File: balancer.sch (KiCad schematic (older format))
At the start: 0 parts

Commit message: added hierarchical sheets and an xh connector
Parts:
- added J1: S4B-XH-SM4-TB, symbol S4B-XH-SM4-TB
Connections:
- new net Cell1+: J1.1
- new net Cell2+: J1.2
- new net Cell3+: J1.3
- new net Cell3-: J1.4
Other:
- note added: "XH Connector"
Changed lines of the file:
@@
 $Descr A4 11693 8268
 encoding utf-8
-Sheet 1 1
+Sheet 1 4
 Title ""
 Date ""
@@
 Comment4 ""
 $EndDescr
+Text Notes 8220 1660 0    60   ~ 0
+XH Connector
+$Sheet
+S 7820 2970 990  380
+U 58CDAE41
+F0 "Cell1" 60
+F1 "CellBalancer.sch" 60
+F2 "Cell+" I R 8810 3040 60
+F3 "Cell-" I R 8810 3280 60
+F4 "Reference" O R 8810 3200 60
+F5 "Undervoltage" O R 8810 3120 60
+$EndSheet
+Text Label 9000 3040 0    60   ~ 0
+Cell1+
+Wire Wire Line
+	8810 3040 9000 3040
+Text Label 8700 1780 2    60   ~ 0
+Cell1+
+Wire Wire Line
+	8700 1780 8760 1780
+$Comp
+L S4B-XH-SM4-TB J1
+U 1 1 58CD24F2
+P 8890 1890
+F 0 "J1" H 8890 2060 60  0000 C CNN
+F 1 "S4B-XH-SM4-TB" H 8870 1680 60  0000 C CNN
+F 2 "" H 8790 1960 60  0001 C CNN
+F 3 "http://www.jst-mfg.com/product/pdf/eng/eXH.pdf" H 8900 1660 60  0001 C CNN
+	1    8890 1890
+	1    0    0    -1
+$EndComp
+$Sheet
+S 7820 3520 990  380
+U 58CDE744
+F0 "Cell2" 60
+F1 "CellBalancer.sch" 60
+F2 "Cell+" I R 8810 3590 60
+F3 "Cell-" I R 8810 3830 60
+F4 "Reference" O R 8810 3750 60
+F5 "Undervoltage" O R 8810 3670 60
+$EndSheet
+Text Label 9000 3590 0    60   ~ 0
+Cell2+
+Wire Wire Line
+	8810 3590 9000 3590
+Wire Wire Line
+	8810 3280 8870 3280
+Wire Wire Line
+	8870 3280 8870 3590
+Connection ~ 8870 3590
+$Sheet
+S 7820 4070 990  380
+U 58CE2F03
+F0 "Cell3" 60
+F1 "CellBalancer.sch" 60
+F2 "Cell+" I R 8810 4140 60
+F3 "Cell-" I R 8810 4380 60
+F4 "Reference" O R 8810 4300 60
+F5 "Undervoltage" O R 8810 4220 60
+$EndSheet
+Text Label 9000 4140 0    60   ~ 0
+Cell3+
+Wire Wire Line
+	9000 4140 8810 4140
+Wire Wire Line
+	8810 3830 8870 3830
+Wire Wire Line
+	8870 3830 8870 4140
+Connection ~ 8870 4140
+Text Label 9000 4380 0    60   ~ 0
+Cell3-
+Wire Wire Line
+	9000 4380 8810 4380
+Text Label 9000 3120 0    60   ~ 0
+Cell1-Undervoltage
+Text Label 9000 3200 0    60   ~ 0
+Cell1-Reference
+Wire Wire Line
+	8810 3120 9000 3120
+Wire Wire Line
+	9000 3200 8810 3200
+Text Label 9000 3670 0    60   ~ 0
+Cell2-Undervoltage
+Text Label 9000 3750 0    60   ~ 0
+Cell2-Reference
+Text Label 9000 4220 0    60   ~ 0
+Cell3-Undervoltage
+Text Label 9000 4300 0    60   ~ 0
+Cell3-Reference
+Wire Wire Line
+	9000 4220 8810 4220
+Wire Wire Line
+	9000 4300 8810 4300
+Wire Wire Line
+	8810 3670 9000 3670
+Wire Wire Line
+	9000 3750 8810 3750
+Text Label 8700 1850 2    60   ~ 0
+Cell2+
+Text Label 8700 1930 2    60   ~ 0
+Cell3+
+Text Label 8700 2000 2    60   ~ 0
+Cell3-
+Wire Wire Line
+	8700 1850 8760 1850
+Wire Wire Line
+	8700 1930 8760 1930
+Wire Wire Line
+	8700 2000 8760 2000
 $EndSCHEMATC

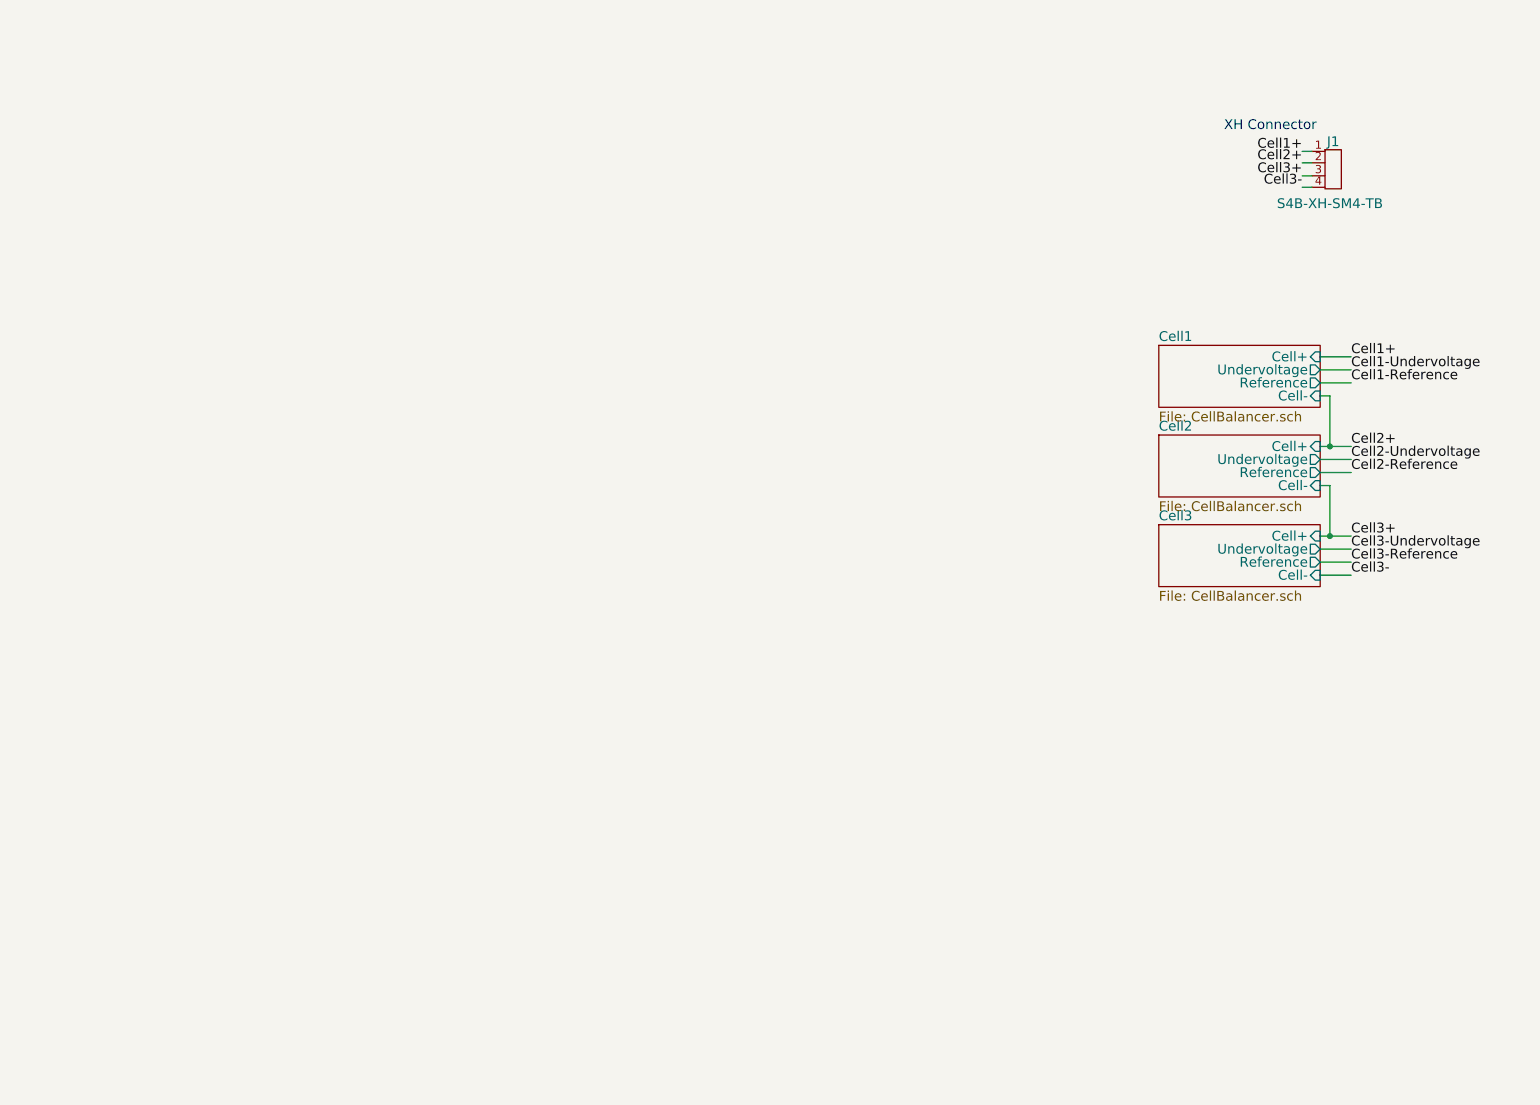
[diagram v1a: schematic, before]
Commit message: high voltage protection done
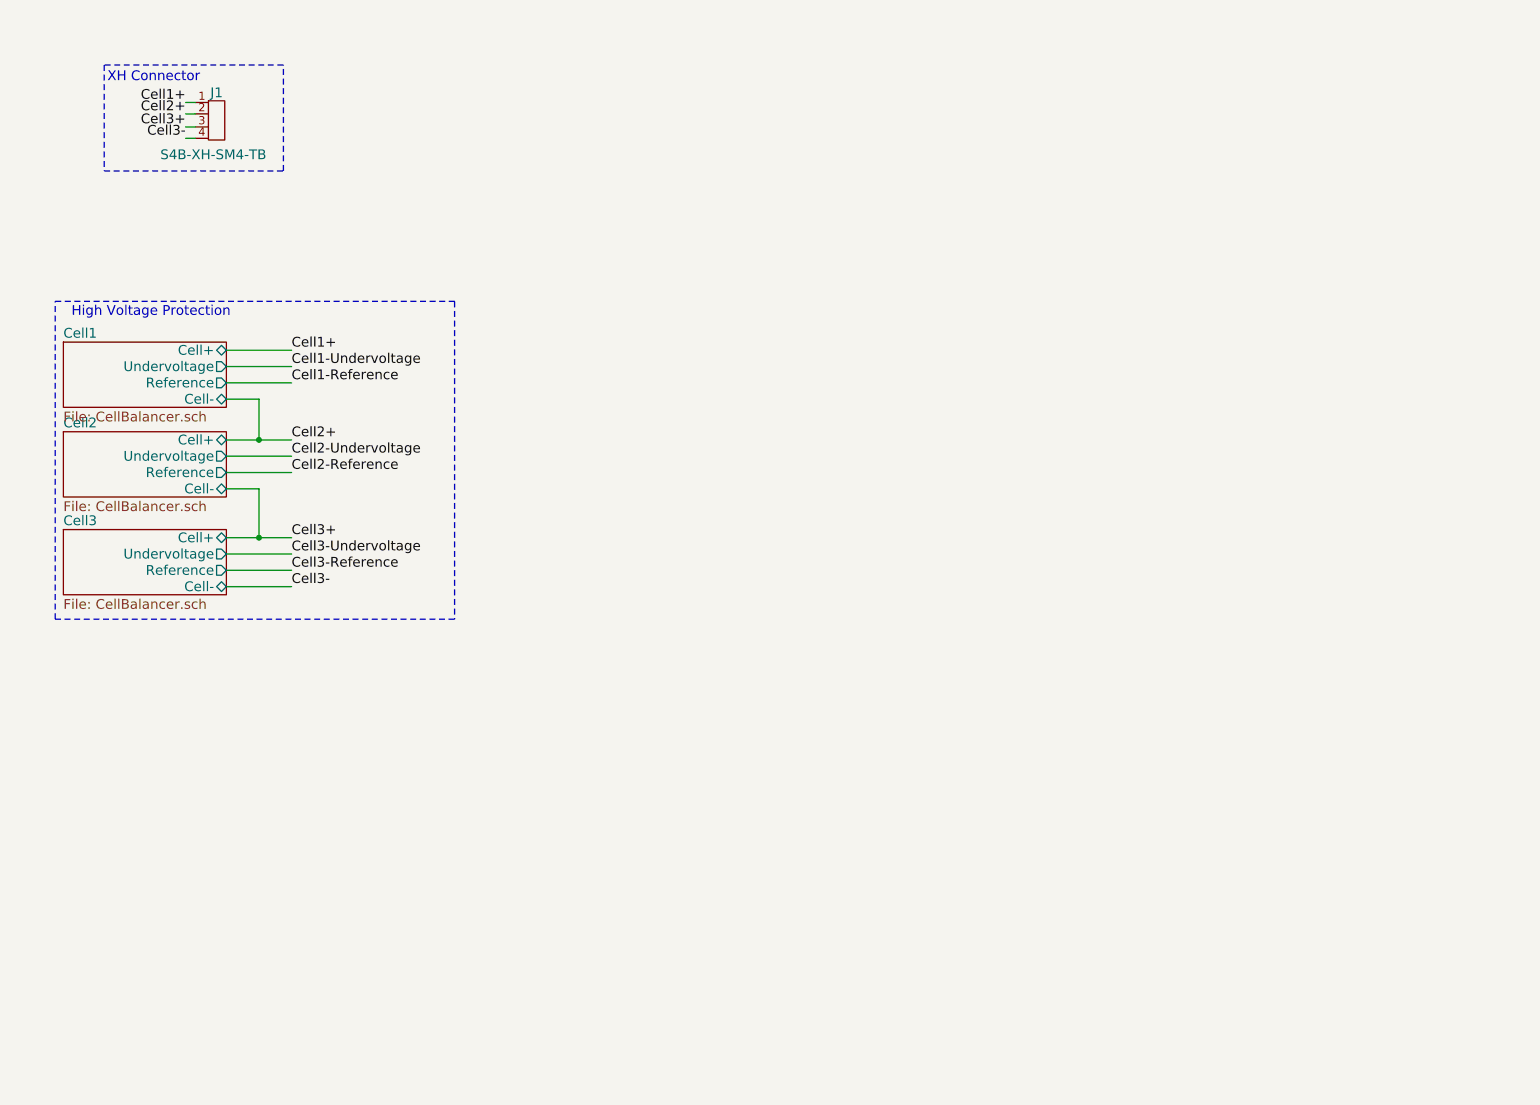
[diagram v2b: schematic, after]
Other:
- note added: "High Voltage Protection"
- moved on the sheet: J1
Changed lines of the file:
@@
 encoding utf-8
 Sheet 1 4
-Title ""
-Date ""
+Title "Balancer"
+Date "2017-03-18"
 Rev ""
 Comp ""
@@
 Comment4 ""
 $EndDescr
-Text Notes 8220 1660 0    60   ~ 0
+Text Notes 1370 1360 0    60   ~ 0
 XH Connector
-$Sheet
-S 7820 2970 990  380
-U 58CDAE41
-F0 "Cell1" 60
-F1 "CellBalancer.sch" 60
-F2 "Cell+" I R 8810 3040 60
-F3 "Cell-" I R 8810 3280 60
-F4 "Reference" O R 8810 3200 60
-F5 "Undervoltage" O R 8810 3120 60
-$EndSheet
-Text Label 9000 3040 0    60   ~ 0
+Text Label 2500 3000 0    60   ~ 0
+Cell1+
+Text Label 1850 1480 2    60   ~ 0
 Cell1+
 Wire Wire Line
-	8810 3040 9000 3040
-Text Label 8700 1780 2    60   ~ 0
-Cell1+
-Wire Wire Line
-	8700 1780 8760 1780
+	1850 1480 1910 1480
 $Comp
 L S4B-XH-SM4-TB J1
 U 1 1 58CD24F2
-P 8890 1890
-F 0 "J1" H 8890 2060 60  0000 C CNN
-F 1 "S4B-XH-SM4-TB" H 8870 1680 60  0000 C CNN
-F 2 "" H 8790 1960 60  0001 C CNN
-F 3 "http://www.jst-mfg.com/product/pdf/eng/eXH.pdf" H 8900 1660 60  0001 C CNN
-	1    8890 1890
+P 2040 1590
+F 0 "J1" H 2040 1760 60  0000 C CNN
+F 1 "S4B-XH-SM4-TB" H 2020 1380 60  0000 C CNN
+F 2 "" H 1940 1660 60  0001 C CNN
+F 3 "http://www.jst-mfg.com/product/pdf/eng/eXH.pdf" H 2050 1360 60  0001 C CNN
+	1    2040 1590
 	1    0    0    -1
 $EndComp
+Text Label 2500 3550 0    60   ~ 0
+Cell2+
+Text Label 2500 4150 0    60   ~ 0
+Cell3+
+Text Label 2500 4450 0    60   ~ 0
+Cell3-
+Text Label 2500 3100 0    60   ~ 0
+Cell1-Undervoltage
+Text Label 2500 3200 0    60   ~ 0
+Cell1-Reference
+Text Label 2500 3650 0    60   ~ 0
+Cell2-Undervoltage
+Text Label 2500 3750 0    60   ~ 0
+Cell2-Reference
+Text Label 2500 4250 0    60   ~ 0
+Cell3-Undervoltage
+Text Label 2500 4350 0    60   ~ 0
+Cell3-Reference
+Text Label 1850 1550 2    60   ~ 0
+Cell2+
+Text Label 1850 1630 2    60   ~ 0
+Cell3+
+Text Label 1850 1700 2    60   ~ 0
+Cell3-
+Wire Wire Line
+	1850 1550 1910 1550
+Wire Wire Line
+	1850 1630 1910 1630
+Wire Wire Line
+	1850 1700 1910 1700
+Wire Notes Line
+	1350 1250 1350 1900
+Wire Notes Line
+	1350 1900 2450 1900
+Wire Notes Line
+	2450 1900 2450 1250
+Wire Notes Line
+	2450 1250 1350 1250
 $Sheet
-S 7820 3520 990  380
-U 58CDE744
+S 1100 2950 1000 400
+U 58CDDC72
+F0 "Cell1" 60
+F1 "CellBalancer.sch" 60
+F2 "Reference" O R 2100 3200 60
+F3 "Undervoltage" O R 2100 3100 60
+F4 "Cell+" B R 2100 3000 60
+F5 "Cell-" B R 2100 3300 60
+$EndSheet
+$Sheet
+S 1100 3500 1000 400
+U 58CDE720
 F0 "Cell2" 60
 F1 "CellBalancer.sch" 60
-F2 "Cell+" I R 8810 3590 60
-F3 "Cell-" I R 8810 3830 60
-F4 "Reference" O R 8810 3750 60
-F5 "Undervoltage" O R 8810 3670 60
+F2 "Reference" O R 2100 3750 60
+F3 "Undervoltage" O R 2100 3650 60
+F4 "Cell+" B R 2100 3550 60
+F5 "Cell-" B R 2100 3850 60
 $EndSheet
-Text Label 9000 3590 0    60   ~ 0
-Cell2+
-Wire Wire Line
-	8810 3590 9000 3590
-Wire Wire Line
-	8810 3280 8870 3280
-Wire Wire Line
-	8870 3280 8870 3590
-Connection ~ 8870 3590
 $Sheet
-S 7820 4070 990  380
-U 58CE2F03
+S 1100 4100 1000 400
+U 58CDEEA6
 F0 "Cell3" 60
 F1 "CellBalancer.sch" 60
-F2 "Cell+" I R 8810 4140 60
-F3 "Cell-" I R 8810 4380 60
-F4 "Reference" O R 8810 4300 60
-F5 "Undervoltage" O R 8810 4220 60
+F2 "Reference" O R 2100 4350 60
+F3 "Undervoltage" O R 2100 4250 60
+F4 "Cell+" B R 2100 4150 60
+F5 "Cell-" B R 2100 4450 60
 $EndSheet
-Text Label 9000 4140 0    60   ~ 0
-Cell3+
 Wire Wire Line
-	9000 4140 8810 4140
+	2100 4450 2500 4450
 Wire Wire Line
-	8810 3830 8870 3830
+	2500 4350 2100 4350
 Wire Wire Line
-	8870 3830 8870 4140
-Connection ~ 8870 4140
-Text Label 9000 4380 0    60   ~ 0
-Cell3-
+	2100 4250 2500 4250
 Wire Wire Line
-	9000 4380 8810 4380
-Text Label 9000 3120 0    60   ~ 0
-Cell1-Undervoltage
-Text Label 9000 3200 0    60   ~ 0
-Cell1-Reference
+	2500 4150 2100 4150
 Wire Wire Line
-	8810 3120 9000 3120
+	2100 3550 2500 3550
 Wire Wire Line
-	9000 3200 8810 3200
-Text Label 9000 3670 0    60   ~ 0
-Cell2-Undervoltage
-Text Label 9000 3750 0    60   ~ 0
-Cell2-Reference
-Text Label 9000 4220 0    60   ~ 0
-Cell3-Undervoltage
-Text Label 9000 4300 0    60   ~ 0
-Cell3-Reference
+	2100 3650 2500 3650
 Wire Wire Line
-	9000 4220 8810 4220
+	2100 3750 2500 3750
 Wire Wire Line
-	9000 4300 8810 4300
+	2100 3850 2300 3850
 Wire Wire Line
-	8810 3670 9000 3670
+	2300 3850 2300 4150
+Connection ~ 2300 4150
 Wire Wire Line
-	9000 3750 8810 3750
-Text Label 8700 1850 2    60   ~ 0
-Cell2+
-Text Label 8700 1930 2    60   ~ 0
-Cell3+
-Text Label 8700 2000 2    60   ~ 0
-Cell3-
+	2100 3300 2300 3300
 Wire Wire Line
-	8700 1850 8760 1850
+	2300 3300 2300 3550
+Connection ~ 2300 3550
 Wire Wire Line
-	8700 1930 8760 1930
+	2100 3200 2500 3200
 Wire Wire Line
-	8700 2000 8760 2000
+	2500 3100 2100 3100
+Wire Wire Line
+	2100 3000 2500 3000
+Wire Notes Line
+	1050 4650 1050 2700
+Wire Notes Line
+	1050 2700 3500 2700
+Wire Notes Line
+	3500 2700 3500 4650
+Wire Notes Line
+	3500 4650 1050 4650
+Text Notes 1150 2800 0    60   ~ 0
+High Voltage Protection
 $EndSCHEMATC

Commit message: schematic done
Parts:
- added IC1: TLV3404, Housings_SOIC:SOIC-14_3.9x8.7mm_Pitch1.27mm, symbol TLV3404
- added J? (x2): CONN_01X01, symbol CONN_01X01
- added Q?: IRF7455PBF, Housings_SOIC:SOIC-8_3.9x4.9mm_Pitch1.27mm, symbol IRF7455PBF
- added R1, R2: 10M, symbol R
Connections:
- net Cell1+: now also IC1.4 (VCC), J?.1 (P1), R1.1, R2.1
- net Cell1-Reference: now also IC1.3 (1IN+)
- net Cell2-Reference: now also IC1.13 (4IN-), IC1.5 (2IN+)
- net Cell3-: now also IC1.11 (GND), Q?.1 (S), Q?.2 (S), Q?.3 (S)
- net Cell3-Reference: now also IC1.10 (3IN+)
- new net: J?.1 (P1), Q?.5 (D), Q?.6 (D), Q?.7 (D), Q?.8 (D)
- new net Cell1-VoltageLow: IC1.2 (1IN-)
- new net Cell2-VoltageLow: IC1.6 (2IN-)
- new net Cell3-VoltageLow: IC1.9 (3IN-)
- new net Global-VoltageLow: IC1.14 (4OUT), Q?.4 (G), R2.2
- new net OpenDrain-VoltageLow: IC1.1 (1OUT), IC1.12 (4IN+), IC1.7 (2OUT), IC1.8 (3OUT), R1.2
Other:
- note added: "Low Voltage Cutout and Output Connectors"
- note added: "Low Voltage Detection"
- moved on the sheet: J1

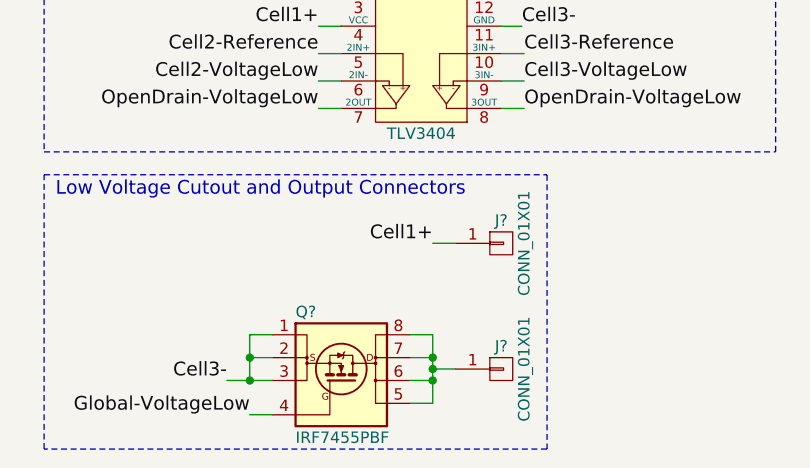
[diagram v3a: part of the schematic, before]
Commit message: added annotations
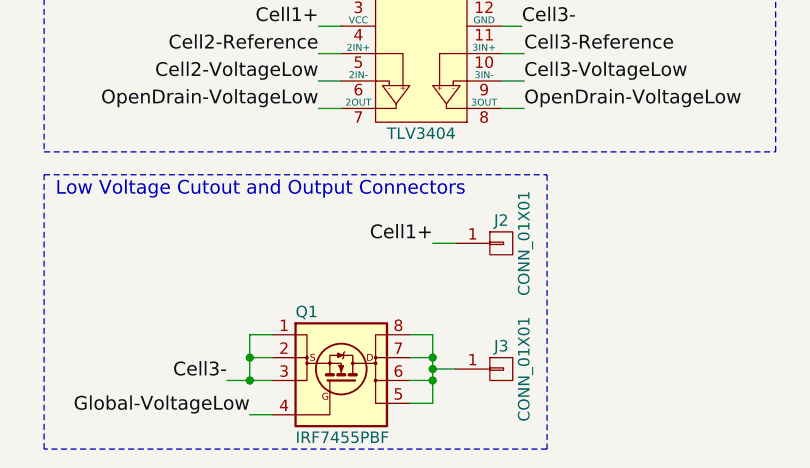
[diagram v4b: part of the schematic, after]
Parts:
- gave numbers to parts that had none: 3
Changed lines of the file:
@@
 Low Voltage Detection
 $Comp
-L IRF7455PBF Q?
+L IRF7455PBF Q1
 U 1 1 58CF30C7
 P 4500 6600
-F 0 "Q?" H 4300 6900 50  0000 L CNN
+F 0 "Q1" H 4300 6900 50  0000 L CNN
 F 1 "IRF7455PBF" H 4300 6350 50  0000 L CNN
 F 2 "Housings_SOIC:SOIC-8_3.9x4.9mm_Pitch1.27mm" H 4510 6190 50  0001 C CIN
@@
 	4200 6750 4100 6750
 $Comp
-L CONN_01X01 J?
+L CONN_01X01 J2
 U 1 1 58CF5086
 P 5200 6000
-F 0 "J?" H 5200 6100 50  0000 C CNN
+F 0 "J2" H 5200 6100 50  0000 C CNN
 F 1 "CONN_01X01" V 5300 6000 50  0000 C CNN
 F 2 "" H 5200 6000 50  0001 C CNN
@@
 $EndComp
 $Comp
-L CONN_01X01 J?
+L CONN_01X01 J3
 U 1 1 58CF5555
 P 5200 6550
-F 0 "J?" H 5200 6650 50  0000 C CNN
+F 0 "J3" H 5200 6650 50  0000 C CNN
 F 1 "CONN_01X01" V 5300 6550 50  0000 C CNN
 F 2 "" H 5200 6550 50  0001 C CNN

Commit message: changed burner resistor to 22R, assigned all footprints
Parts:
- J1: footprint (none) -> balancer:JST_XH_S4B-XH-SM4-TB_04x2.50mm_Angled
- J2, J3: footprint (none) -> Pin_Headers:Pin_Header_Straight_1x01_Pitch2.54mm
- R1, R2: footprint (none) -> Resistors_SMD:R_0805_HandSoldering
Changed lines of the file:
@@
 F 0 "J1" H 3890 1760 60  0000 C CNN
 F 1 "S4B-XH-SM4-TB" H 3870 1380 60  0000 C CNN
-F 2 "" H 3790 1660 60  0001 C CNN
+F 2 "balancer:JST_XH_S4B-XH-SM4-TB_04x2.50mm_Angled" H 3790 1660 60  0001 C CNN
 F 3 "http://www.jst-mfg.com/product/pdf/eng/eXH.pdf" H 3900 1360 60  0001 C CNN
 	1    3890 1590
@@
 F 0 "R1" V 4480 4450 50  0000 C CNN
 F 1 "10M" V 4400 4450 50  0000 C CNN
-F 2 "" V 4330 4450 50  0001 C CNN
+F 2 "Resistors_SMD:R_0805_HandSoldering" V 4330 4450 50  0001 C CNN
 F 3 "" H 4400 4450 50  0001 C CNN
 	1    4400 4450
@@
 F 0 "R2" V 5380 4450 50  0000 C CNN
 F 1 "10M" V 5300 4450 50  0000 C CNN
-F 2 "" V 5230 4450 50  0001 C CNN
+F 2 "Resistors_SMD:R_0805_HandSoldering" V 5230 4450 50  0001 C CNN
 F 3 "" H 5300 4450 50  0001 C CNN
 	1    5300 4450
@@
 F 0 "J2" H 5200 6100 50  0000 C CNN
 F 1 "CONN_01X01" V 5300 6000 50  0000 C CNN
-F 2 "" H 5200 6000 50  0001 C CNN
+F 2 "Pin_Headers:Pin_Header_Straight_1x01_Pitch2.54mm" H 5200 6000 50  0001 C CNN
 F 3 "" H 5200 6000 50  0001 C CNN
 	1    5200 6000
@@
 F 0 "J3" H 5200 6650 50  0000 C CNN
 F 1 "CONN_01X01" V 5300 6550 50  0000 C CNN
-F 2 "" H 5200 6550 50  0001 C CNN
+F 2 "Pin_Headers:Pin_Header_Straight_1x01_Pitch2.54mm" H 5200 6550 50  0001 C CNN
 F 3 "" H 5200 6550 50  0001 C CNN
 	1    5200 6550

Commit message: Front side pcb first version
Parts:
- R1, R2: footprint Resistors_SMD:R_0805_HandSoldering -> Resistors_SMD:R_0805
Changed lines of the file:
@@
 F 0 "R1" V 4480 4450 50  0000 C CNN
 F 1 "10M" V 4400 4450 50  0000 C CNN
-F 2 "Resistors_SMD:R_0805_HandSoldering" V 4330 4450 50  0001 C CNN
+F 2 "Resistors_SMD:R_0805" V 4330 4450 50  0001 C CNN
 F 3 "" H 4400 4450 50  0001 C CNN
 	1    4400 4450
@@
 F 0 "R2" V 5380 4450 50  0000 C CNN
 F 1 "10M" V 5300 4450 50  0000 C CNN
-F 2 "Resistors_SMD:R_0805_HandSoldering" V 5230 4450 50  0001 C CNN
+F 2 "Resistors_SMD:R_0805" V 5230 4450 50  0001 C CNN
 F 3 "" H 5300 4450 50  0001 C CNN
 	1    5300 4450

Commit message: layout finalized
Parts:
- added D7: LED, LEDs:LED_0805, symbol LED
- added J4: Input (+), balancer:Solder_Terminal_4x4mm, symbol CONN_01X01
- added J5: Input (-), balancer:Solder_Terminal_4x4mm, symbol CONN_01X01
- added R27: 680R, Resistors_SMD:R_0805, symbol R
- J2: value CONN_01X01 -> Output (+); footprint Pin_Headers:Pin_Header_Straight_1x01_Pitch2.54mm -> balancer:Solder_Terminal_4x4mm
- J3: value CONN_01X01 -> Output (-); footprint Pin_Headers:Pin_Header_Straight_1x01_Pitch2.54mm -> balancer:Solder_Terminal_4x4mm
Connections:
- net Cell1+: now also R2.2, J4.1 (P1), R27.1; no longer R2.1
- net Cell2-Reference: now also IC1.9 (3IN-); no longer IC1.13 (4IN-)
- net Cell3-: now also J5.1 (P1)
- net Cell3-Reference: now also IC1.12 (4IN+); no longer IC1.10 (3IN+)
- net Cell3-VoltageLow: now also IC1.13 (4IN-); no longer IC1.9 (3IN-)
- net Global-VoltageLow: now also IC1.8 (3OUT), R2.1; no longer IC1.14 (4OUT), R2.2
- net OpenDrain-VoltageLow: now also IC1.10 (3IN+), IC1.14 (4OUT); no longer IC1.12 (4IN+), IC1.8 (3OUT)
- net Output-: now reaches J3.1 (P1), Q1.5 (D), Q1.6 (D), Q1.7 (D), Q1.8 (D)
- net Output-: now also D7.1 (K)
- new net: D7.2 (A), R27.2
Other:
- note added: "Input Connectors"
- note added: "Low Voltage Cutout"
- note added: "Output Connectors"
- note added: "Output LED"
- note removed: "Low Voltage Cutout and Output Connectors"
- note removed: "XH Connector"
- moved on the sheet: IC1, J1, J2, J3, Q1, R1, R2
